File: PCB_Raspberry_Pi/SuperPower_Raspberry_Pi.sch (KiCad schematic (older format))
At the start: 1 part, among them J1 RPi_GPIO

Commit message: test_library
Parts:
- added U?: LH0002H, Package_TO_SOT_THT:TO-5-8, symbol SuperPower_Library:LH0002H
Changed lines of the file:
@@
 Wire Wire Line
 	6200 4300 6150 4300
+$Comp
+L SuperPower_Library:LH0002H U?
+U 1 1 5F4FF601
+P 3650 3200
+F 0 "U?" H 3420 3302 50  0000 R CNN
+F 1 "LH0002H" H 3420 3211 50  0000 R CNN
+F 2 "Package_TO_SOT_THT:TO-5-8" H 3650 3200 50  0001 C CNN
+F 3 "" H 3650 3200 50  0001 C CNN
+	1    3650 3200
+	1    0    0    -1
+$EndComp
 $EndSCHEMATC

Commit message: libraries organized
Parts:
- removed U?: LH0002H, Package_TO_SOT_THT:TO-5-8, symbol SuperPower_Library:LH0002H
- added H?: MountingHole, symbol Mechanical:MountingHole
- J1: symbol Connector_Generic:Conn_02x20_Odd_Even -> SuperPower_Library:Raspberry_Pi_GPIO_Header
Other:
- moved on the sheet: J1
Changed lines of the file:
@@
 EESchema Schematic File Version 4
+LIBS:SuperPower_Raspberry_Pi-cache
 EELAYER 26 0
 EELAYER END
@@
 $EndDescr
 $Comp
-L Connector_Generic:Conn_02x20_Odd_Even J1
+L SuperPower_Library:Raspberry_Pi_GPIO_Header J1
 U 1 1 5C3DC065
-P 6400 3600
-F 0 "J1" H 6450 2450 60  0000 C CNN
-F 1 "RPi_GPIO" H 6450 2350 60  0000 C CNN
-F 2 "Connector_PinSocket_2.54mm:PinSocket_2x20_P2.54mm_Vertical" H 7550 3600 60  0001 C CNN
-F 3 "" H 6400 3600 60  0000 C CNN
-	1    6400 3600
+P 6050 4200
+F 0 "J1" H 6050 5300 60  0000 C CNN
+F 1 "RPi_GPIO" H 6050 3000 60  0000 C CNN
+F 2 "Connector_PinSocket_2.54mm:PinSocket_2x20_P2.54mm_Vertical" H 7200 4200 60  0001 C CNN
+F 3 "" H 6050 4200 60  0000 C CNN
+	1    6050 4200
 	1    0    0    -1
 $EndComp
-Text GLabel 6000 2800 0    50   Input ~ 0
+Text GLabel 5400 3400 0    50   Input ~ 0
 SDA
-Text GLabel 6000 2900 0    50   Input ~ 0
+Text GLabel 5400 3500 0    50   Input ~ 0
 SCL
 Wire Wire Line
-	6000 2800 6200 2800
+	5400 3400 5600 3400
 Wire Wire Line
-	6000 2900 6200 2900
+	5400 3500 5600 3500
 $Comp
 L power:+3.3V #PWR0106
 U 1 1 5C3DD62D
-P 5550 2600
-F 0 "#PWR0106" H 5550 2450 50  0001 C CNN
-F 1 "+3.3V" H 5565 2773 50  0000 C CNN
-F 2 "" H 5550 2600 50  0001 C CNN
-F 3 "" H 5550 2600 50  0001 C CNN
-	1    5550 2600
+P 4950 3200
+F 0 "#PWR0106" H 4950 3050 50  0001 C CNN
+F 1 "+3.3V" H 4965 3373 50  0000 C CNN
+F 2 "" H 4950 3200 50  0001 C CNN
+F 3 "" H 4950 3200 50  0001 C CNN
+	1    4950 3200
 	1    0    0    -1
 $EndComp
 Wire Wire Line
-	6200 2700 5550 2700
+	5600 3300 4950 3300
 Wire Wire Line
-	5550 2700 5550 2600
+	4950 3300 4950 3200
 $Comp
 L power:GND #PWR0108
 U 1 1 5C3DDE65
-P 5350 3250
-F 0 "#PWR0108" H 5350 3000 50  0001 C CNN
-F 1 "GND" H 5355 3077 50  0000 C CNN
-F 2 "" H 5350 3250 50  0001 C CNN
-F 3 "" H 5350 3250 50  0001 C CNN
-	1    5350 3250
+P 4750 3850
+F 0 "#PWR0108" H 4750 3600 50  0001 C CNN
+F 1 "GND" H 4755 3677 50  0000 C CNN
+F 2 "" H 4750 3850 50  0001 C CNN
+F 3 "" H 4750 3850 50  0001 C CNN
+	1    4750 3850
 	1    0    0    -1
 $EndComp
 Wire Wire Line
-	6200 3100 5350 3100
+	5600 3700 4750 3700
 Wire Wire Line
-	5350 3100 5350 3250
+	4750 3700 4750 3850
 $Comp
 L power:GND #PWR0107
 U 1 1 5CDAA9DB
-P 5900 3950
-F 0 "#PWR0107" H 5900 3700 50  0001 C CNN
-F 1 "GND" H 5905 3777 50  0000 C CNN
-F 2 "" H 5900 3950 50  0001 C CNN
-F 3 "" H 5900 3950 50  0001 C CNN
-	1    5900 3950
+P 5300 4550
+F 0 "#PWR0107" H 5300 4300 50  0001 C CNN
+F 1 "GND" H 5305 4377 50  0000 C CNN
+F 2 "" H 5300 4550 50  0001 C CNN
+F 3 "" H 5300 4550 50  0001 C CNN
+	1    5300 4550
 	1    0    0    -1
 $EndComp
 Wire Wire Line
-	6200 3900 5900 3900
+	5600 4500 5300 4500
 Wire Wire Line
-	5900 3900 5900 3950
+	5300 4500 5300 4550
 $Comp
 L power:+5V #PWR0114
 U 1 1 5CE134C5
-P 6850 2500
-F 0 "#PWR0114" H 6850 2350 50  0001 C CNN
-F 1 "+5V" H 6865 2673 50  0000 C CNN
-F 2 "" H 6850 2500 50  0001 C CNN
-F 3 "" H 6850 2500 50  0001 C CNN
-	1    6850 2500
+P 6650 3100
+F 0 "#PWR0114" H 6650 2950 50  0001 C CNN
+F 1 "+5V" H 6665 3273 50  0000 C CNN
+F 2 "" H 6650 3100 50  0001 C CNN
+F 3 "" H 6650 3100 50  0001 C CNN
+	1    6650 3100
 	1    0    0    -1
 $EndComp
 Wire Wire Line
-	6850 2500 6850 2700
+	6650 3100 6650 3300
 Wire Wire Line
-	6850 2800 6700 2800
+	6650 3400 6500 3400
 Wire Wire Line
-	6700 2700 6850 2700
-Connection ~ 6850 2700
+	6500 3300 6650 3300
+Connection ~ 6650 3300
 Wire Wire Line
-	6850 2700 6850 2800
+	6650 3300 6650 3400
 Wire Wire Line
-	6200 4300 6150 4300
+	5600 4900 5550 4900
 $Comp
-L SuperPower_Library:LH0002H U?
-U 1 1 5F4FF601
-P 3650 3200
-F 0 "U?" H 3420 3302 50  0000 R CNN
-F 1 "LH0002H" H 3420 3211 50  0000 R CNN
-F 2 "Package_TO_SOT_THT:TO-5-8" H 3650 3200 50  0001 C CNN
-F 3 "" H 3650 3200 50  0001 C CNN
-	1    3650 3200
+L Mechanical:MountingHole H?
+U 1 1 5F4EFF6E
+P 600 7650
+F 0 "H?" H 700 7696 50  0000 L CNN
+F 1 "MountingHole" H 700 7605 50  0000 L CNN
+F 2 "" H 600 7650 50  0001 C CNN
+F 3 "~" H 600 7650 50  0001 C CNN
+	1    600  7650
 	1    0    0    -1
 $EndComp

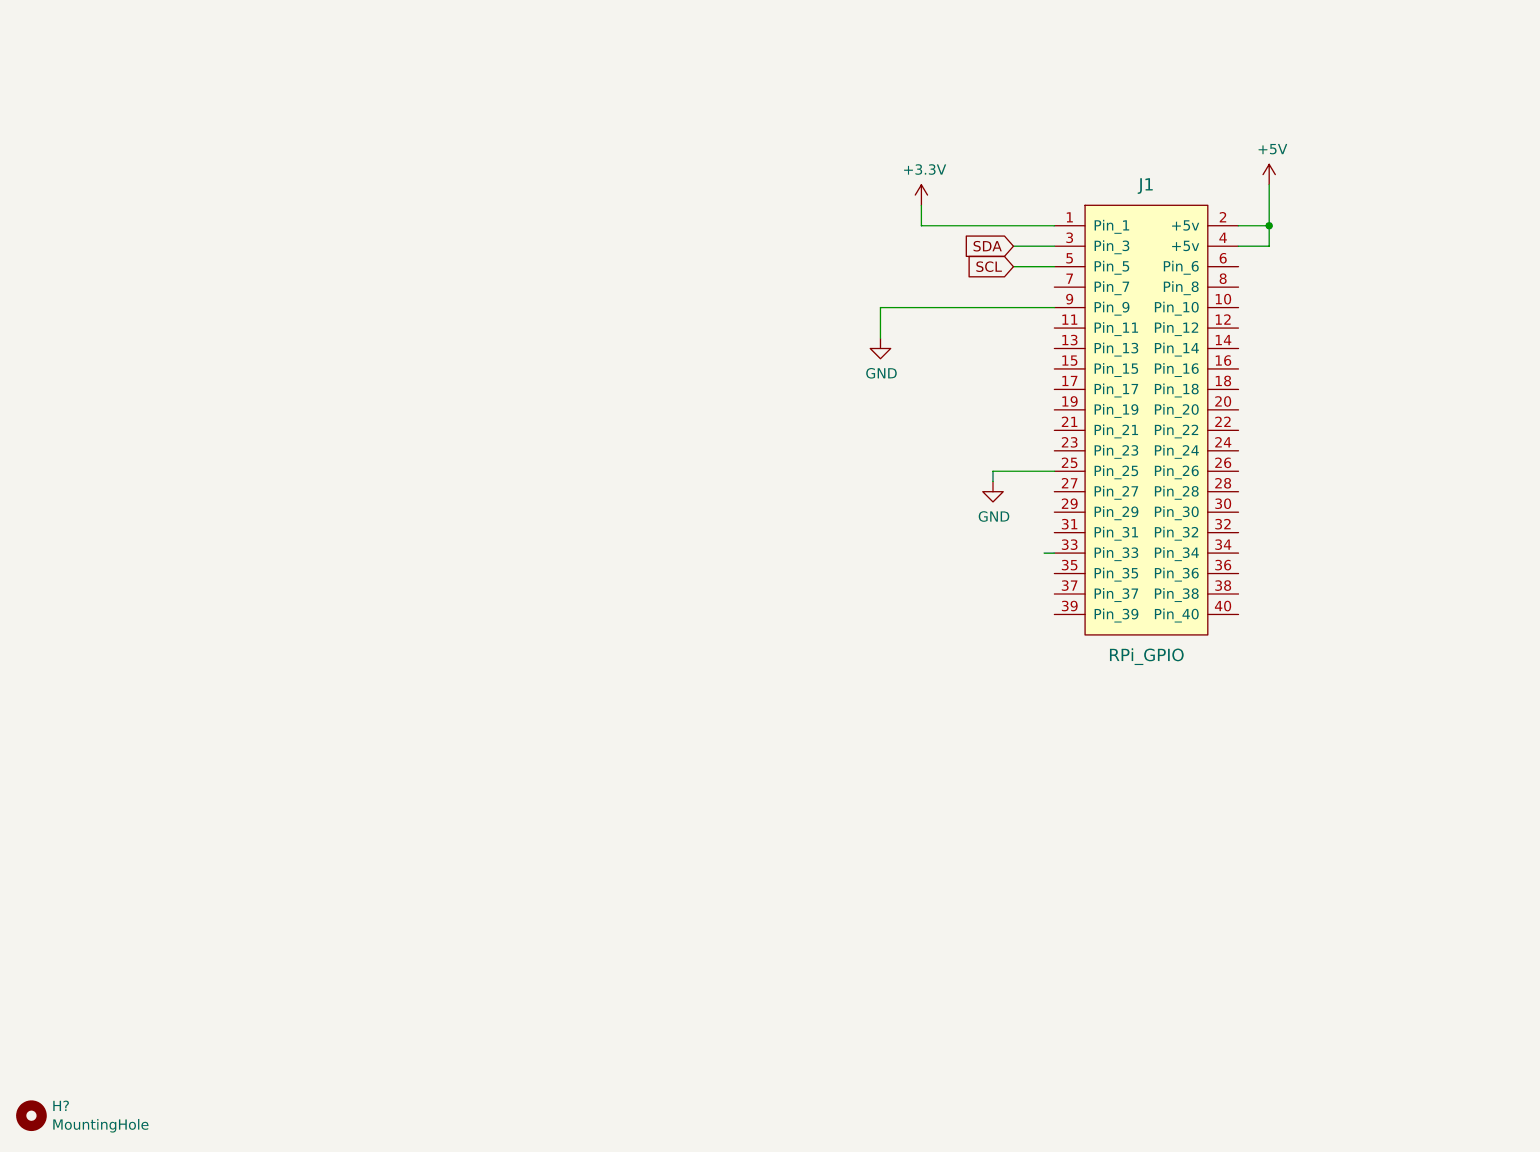
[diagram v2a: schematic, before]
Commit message: script for export BOM
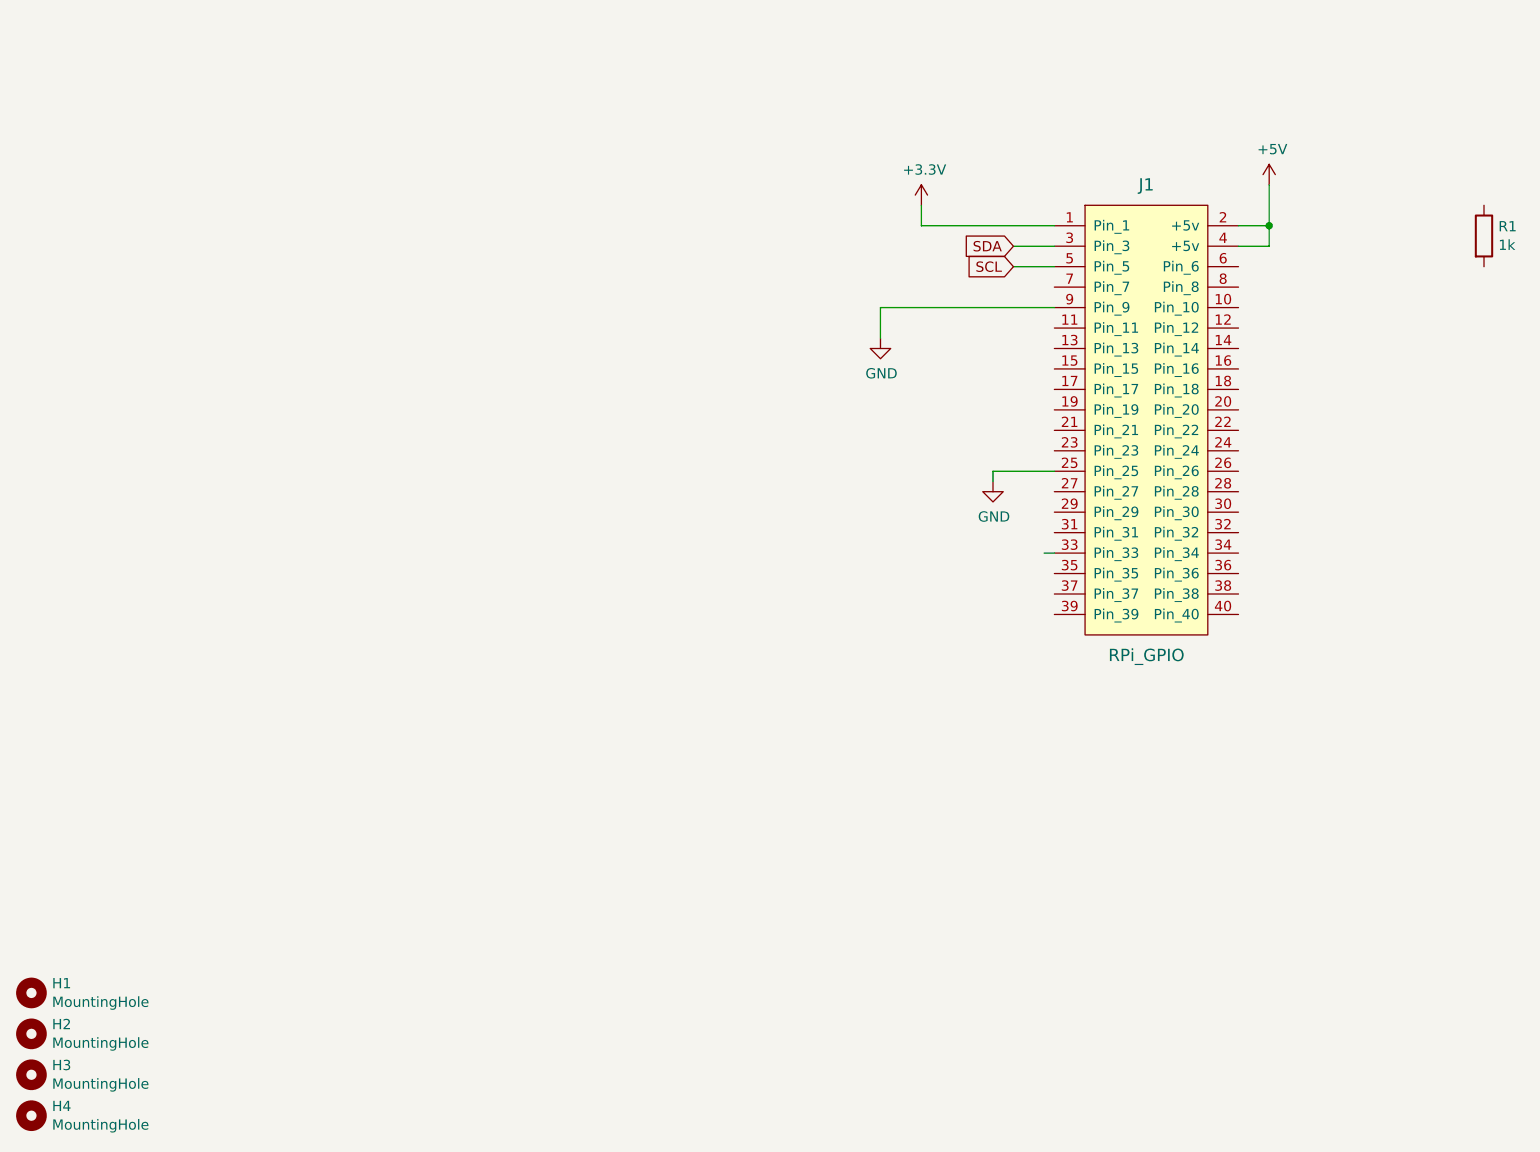
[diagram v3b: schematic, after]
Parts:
- added H2, H3, H4: MountingHole, SuperPower_Library:RPi_Hat_Mounting_Hole, symbol Mechanical:MountingHole
- added R1: 1k, Resistor_SMD:R_0805_2012Metric, symbol Device:R
- H1: renamed from H?; footprint (none) -> SuperPower_Library:RPi_Hat_Mounting_Hole; Keys (none) -> EXCLUDE
- J1: Keys (none) -> DNP
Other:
- moved on the sheet: H1
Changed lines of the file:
@@
 EESchema Schematic File Version 4
-LIBS:SuperPower_Raspberry_Pi-cache
-EELAYER 26 0
+EELAYER 30 0
 EELAYER END
 $Descr A4 11693 8268
@@
 F 2 "Connector_PinSocket_2.54mm:PinSocket_2x20_P2.54mm_Vertical" H 7200 4200 60  0001 C CNN
 F 3 "" H 6050 4200 60  0000 C CNN
+F 4 "DNP" H 6050 4200 50  0001 C CNN "Keys"
 	1    6050 4200
 	1    0    0    -1
@@
 	5600 4900 5550 4900
 $Comp
-L Mechanical:MountingHole H?
+L Mechanical:MountingHole H1
 U 1 1 5F4EFF6E
+P 600 7050
+F 0 "H1" H 700 7096 50  0000 L CNN
+F 1 "MountingHole" H 700 7005 50  0000 L CNN
+F 2 "SuperPower_Library:RPi_Hat_Mounting_Hole" H 600 7050 50  0001 C CNN
+F 3 "~" H 600 7050 50  0001 C CNN
+F 4 "EXCLUDE" H 600 7050 50  0001 C CNN "Keys"
+	1    600  7050
+	1    0    0    -1
+$EndComp
+$Comp
+L Device:R R1
+U 1 1 5F517D74
+P 7700 3350
+F 0 "R1" H 7770 3396 50  0000 L CNN
+F 1 "1k" H 7770 3305 50  0000 L CNN
+F 2 "Resistor_SMD:R_0805_2012Metric" V 7630 3350 50  0001 C CNN
+F 3 "~" H 7700 3350 50  0001 C CNN
+F 4 "C17513" H 7700 3350 50  0001 C CNN "PartNumber"
+	1    7700 3350
+	1    0    0    -1
+$EndComp
+$Comp
+L Mechanical:MountingHole H2
+U 1 1 5F5173E0
+P 600 7250
+F 0 "H2" H 700 7296 50  0000 L CNN
+F 1 "MountingHole" H 700 7205 50  0000 L CNN
+F 2 "SuperPower_Library:RPi_Hat_Mounting_Hole" H 600 7250 50  0001 C CNN
+F 3 "~" H 600 7250 50  0001 C CNN
+F 4 "EXCLUDE" H 600 7250 50  0001 C CNN "Keys"
+	1    600  7250
+	1    0    0    -1
+$EndComp
+$Comp
+L Mechanical:MountingHole H3
+U 1 1 5F51765D
+P 600 7450
+F 0 "H3" H 700 7496 50  0000 L CNN
+F 1 "MountingHole" H 700 7405 50  0000 L CNN
+F 2 "SuperPower_Library:RPi_Hat_Mounting_Hole" H 600 7450 50  0001 C CNN
+F 3 "~" H 600 7450 50  0001 C CNN
+F 4 "EXCLUDE" H 600 7450 50  0001 C CNN "Keys"
+	1    600  7450
+	1    0    0    -1
+$EndComp
+$Comp
+L Mechanical:MountingHole H4
+U 1 1 5F517922
 P 600 7650
-F 0 "H?" H 700 7696 50  0000 L CNN
+F 0 "H4" H 700 7696 50  0000 L CNN
 F 1 "MountingHole" H 700 7605 50  0000 L CNN
-F 2 "" H 600 7650 50  0001 C CNN
+F 2 "SuperPower_Library:RPi_Hat_Mounting_Hole" H 600 7650 50  0001 C CNN
 F 3 "~" H 600 7650 50  0001 C CNN
+F 4 "EXCLUDE" H 600 7650 50  0001 C CNN "Keys"
 	1    600  7650
 	1    0    0    -1
